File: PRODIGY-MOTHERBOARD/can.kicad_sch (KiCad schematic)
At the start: 13 parts, among them U4 TJA1051T-E

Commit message: Motherboard PCB layout started
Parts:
- removed FID11, FID12: Fiducial, Fiducial:Fiducial_1mm_Mask3mm, symbol Mechanical:Fiducial
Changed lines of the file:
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@@
-	)
-	(symbol
-		(lib_id "Mechanical:Fiducial")
-		(at 133.35 121.92 0)
-		(unit 1)
-		(exclude_from_sim no)
-		(in_bom yes)
-		(on_board yes)
-		(dnp yes)
-		(fields_autoplaced yes)
-		(property "Reference" "FID11"
-			(at 135.89 120.6499 0)
-			(effects
-				(font
-					(size 1.27 1.27)
-				)
-				(justify left)
-			)
-		)
-		(property "Value" "Fiducial"
-			(at 135.89 123.1899 0)
-			(effects
-				(font
-					(size 1.27 1.27)
-				)
-				(justify left)
-			)
-		)
-		(property "Footprint" "Fiducial:Fiducial_1mm_Mask3mm"
-			(at 133.35 121.92 0)
-			(effects
-				(font
-					(size 1.27 1.27)
-				)
-				(hide yes)
-			)
-		)
-		(property "Datasheet" "~"
-			(at 133.35 121.92 0)
-			(effects
-				(font
-					(size 1.27 1.27)
-				)
-				(hide yes)
-			)
-		)
-		(property "Description" "Fiducial Marker"
-			(at 133.35 121.92 0)
-			(effects
-				(font
-					(size 1.27 1.27)
-				)
-				(hide yes)
-			)
-		)
-		(property "MOUSER" ""
-			(at 133.35 121.92 0)
-			(effects
-				(font
-					(size 1.27 1.27)
-				)
-				(hide yes)
-			)
-		)
-		(property "Sim.Type" ""
-			(at 133.35 121.92 0)
-			(effects
-				(font
-					(size 1.27 1.27)
-				)
-				(hide yes)
-			)
-		)
-		(property "TME" ""
-			(at 133.35 121.92 0)
-			(effects
-				(font
-					(size 1.27 1.27)
-				)
-				(hide yes)
-			)
-		)
-		(instances
-			(project "PRODIGY-MOTHERBOARD"
-				(path "/f1c25860-8989-4190-bd24-2491d23ca7d9/cf0d8bf1-4632-49df-9398-b3de35528304"
-					(reference "FID11")
-					(unit 1)
-				)
-			)
-		)
 	)
 	(symbol
@@
 					(unit 1)
 				)
-			)
-		)
-	)
-	(symbol
-		(lib_id "Mechanical:Fiducial")
-		(at 133.35 127 0)
-		(unit 1)
-		(exclude_from_sim no)
-		(in_bom yes)
-		(on_board yes)
-		(dnp yes)
-		(fields_autoplaced yes)
-		(property "Reference" "FID12"
-			(at 135.89 125.7299 0)
-			(effects
-				(font
-					(size 1.27 1.27)
-				)
-				(justify left)
-			)
-		)
-		(property "Value" "Fiducial"
-			(at 135.89 128.2699 0)
-			(effects
-				(font
-					(size 1.27 1.27)
-				)
-				(justify left)
-			)
-		)
-		(property "Footprint" "Fiducial:Fiducial_1mm_Mask3mm"
-			(at 133.35 127 0)
-			(effects
-				(font
-					(size 1.27 1.27)
-				)
-				(hide yes)
-			)
-		)
-		(property "Datasheet" "~"
-			(at 133.35 127 0)
-			(effects
-				(font
-					(size 1.27 1.27)
-				)
-				(hide yes)
-			)
-		)
-		(property "Description" "Fiducial Marker"
-			(at 133.35 127 0)
-			(effects
-				(font
-					(size 1.27 1.27)
-				)
-				(hide yes)
-			)
-		)
-		(property "MOUSER" ""
-			(at 133.35 127 0)
-			(effects
-				(font
-					(size 1.27 1.27)
-				)
-				(hide yes)
-			)
-		)
-		(property "Sim.Type" ""
-			(at 133.35 127 0)
-			(effects
-				(font
-					(size 1.27 1.27)
-				)
-				(hide yes)
-			)
-		)
-		(property "TME" ""
-			(at 133.35 127 0)
-			(effects
-				(font
-					(size 1.27 1.27)
-				)
-				(hide yes)
-			)
-		)
-		(instances
-			(project "PRODIGY-MOTHERBOARD"
-				(path "/f1c25860-8989-4190-bd24-2491d23ca7d9/cf0d8bf1-4632-49df-9398-b3de35528304"
-					(reference "FID12")
-					(unit 1)
-				)

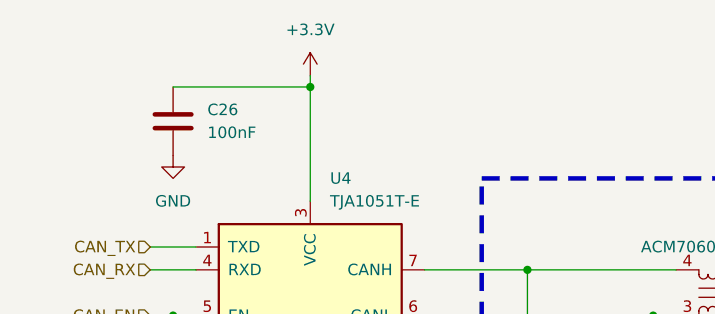
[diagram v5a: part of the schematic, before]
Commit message: Power routing done...not nicely tho
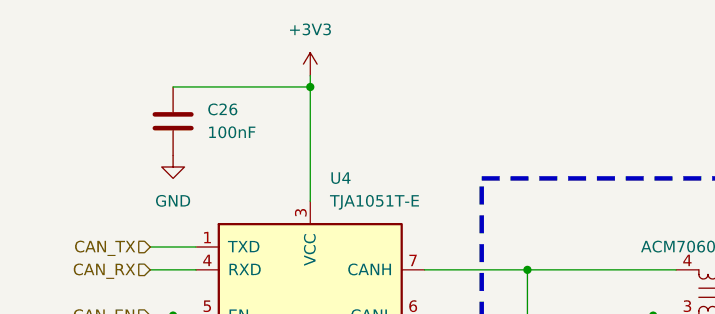
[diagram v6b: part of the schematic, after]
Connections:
- net +3.3V renamed +3V3
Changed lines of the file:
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@@
+	)
+	(symbol
+		(lib_id "power:+3V3")
+		(at 110.49 64.77 0)
+		(unit 1)
+		(exclude_from_sim no)
+		(in_bom yes)
+		(on_board yes)
+		(dnp no)
+		(fields_autoplaced yes)
+		(property "Reference" "#PWR061"
+			(at 110.49 68.58 0)
+			(effects
+				(font
+					(size 1.27 1.27)
+				)
+				(hide yes)
+			)
+		)
+		(property "Value" "+3V3"
+			(at 110.49 59.69 0)
+			(effects
+				(font
+					(size 1.27 1.27)
+				)
+			)
+		)
+		(property "Footprint" ""
+			(at 110.49 64.77 0)
+			(effects
+				(font
+					(size 1.27 1.27)
+				)
+				(hide yes)
+			)
+		)
+		(property "Datasheet" ""
+			(at 110.49 64.77 0)
+			(effects
+				(font
+					(size 1.27 1.27)
+				)
+				(hide yes)
+			)
+		)
+		(property "Description" "Power symbol creates a global label with name \"+3V3\""
+			(at 110.49 64.77 0)
+			(effects
+				(font
+					(size 1.27 1.27)
+				)
+				(hide yes)
+			)
+		)
+		(pin "1"
+		)
+		(instances
+			(project "PRODIGY-MOTHERBOARD"
+				(path "/f1c25860-8989-4190-bd24-2491d23ca7d9/cf0d8bf1-4632-49df-9398-b3de35528304"
+					(reference "#PWR061")
+					(unit 1)
+				)
+			)
+		)
 	)
 	(symbol
@@
 					(unit 1)
 				)
-			)
-		)
-	)
-	(symbol
-		(lib_id "power:+3.3V")
-		(at 110.49 64.77 0)
-		(unit 1)
-		(exclude_from_sim no)
-		(in_bom yes)
-		(on_board yes)
-		(dnp no)
-		(fields_autoplaced yes)
-		(property "Reference" "#PWR061"
-			(at 110.49 68.58 0)
-			(effects
-				(font
-					(size 1.27 1.27)
-				)
-				(hide yes)
-			)
-		)
-		(property "Value" "+3.3V"
-			(at 110.49 59.69 0)
-			(effects
-				(font
-					(size 1.27 1.27)
-				)
-			)
-		)
-		(property "Footprint" ""
-			(at 110.49 64.77 0)
-			(effects
-				(font
-					(size 1.27 1.27)
-				)
-				(hide yes)
-			)
-		)
-		(property "Datasheet" ""
-			(at 110.49 64.77 0)
-			(effects
-				(font
-					(size 1.27 1.27)
-				)
-				(hide yes)
-			)
-		)
-		(property "Description" "Power symbol creates a global label with name \"+3.3V\""
-			(at 110.49 64.77 0)
-			(effects
-				(font
-					(size 1.27 1.27)
-				)
-				(hide yes)
-			)
-		)
-		(pin "1"
-		)
-		(instances
-			(project "PRODIGY-MOTHERBOARD"
-				(path "/f1c25860-8989-4190-bd24-2491d23ca7d9/cf0d8bf1-4632-49df-9398-b3de35528304"
-					(reference "#PWR061")
-					(unit 1)
-				)
